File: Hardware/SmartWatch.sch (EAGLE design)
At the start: 99 parts, among them IC1 BQ25180YBGR, IC2 DRV2605YZFR, IC3 BMA421, IC9 RT6160AWSC, J1 503480-2400, J2 TC2030-IDC, J4 KH-TYPE-C-16P, Q1 20V/4.2A/52mΩ/1.4W, Q3 SI1308EDL-T1-GE3, U1 NRF52840_QF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

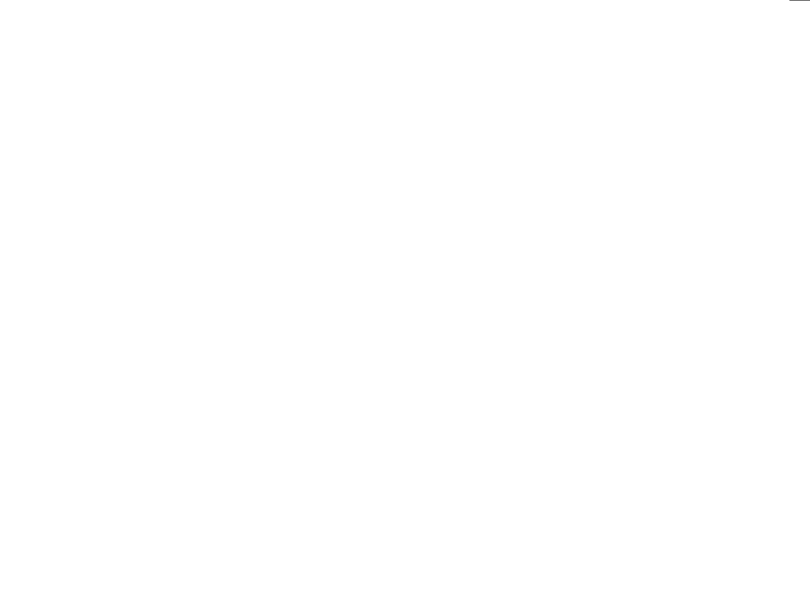
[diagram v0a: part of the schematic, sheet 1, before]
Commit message: Added the missing pads
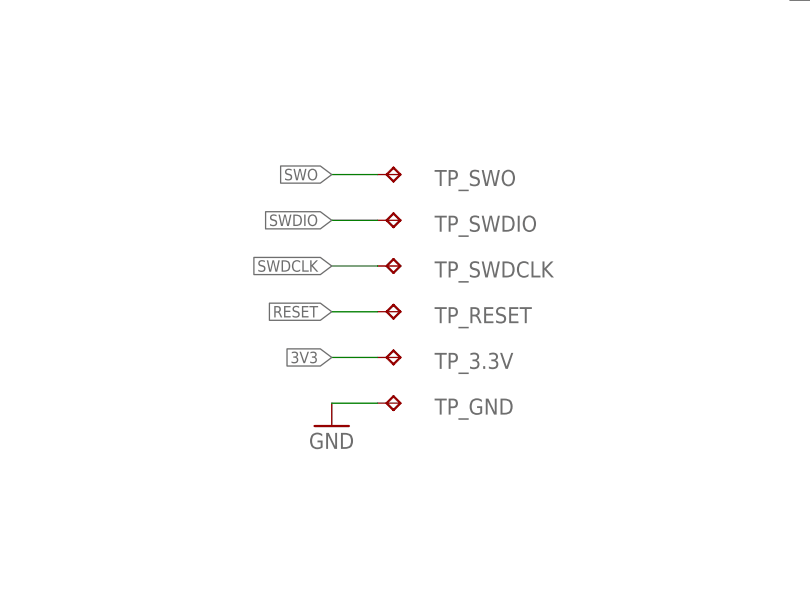
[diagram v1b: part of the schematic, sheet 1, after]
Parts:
- added TP_3.3V, TP_GND, TP_RESET, TP_SWDCLK, TP_SWDIO, TP_SWO: HECTOR_WATCH_1_TPTP20R, InkTime_v5:HECTOR_WATCH_1_TPTP20R
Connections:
- net 3V3: now also TP_3.3V.TP
- net GND: now also TP_GND.TP
- net RESET: now also TP_RESET.TP
- net SWDCLK: now also TP_SWDCLK.TP
- net SWDIO: now also TP_SWDIO.TP
- net SWO: now also TP_SWO.TP
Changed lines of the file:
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@@
 <part name="FRAME1" library="InkTime_v5" library_urn="urn:adsk.wipprod:fs.file:vf.a-hroK1ETJmXGG-M9gXLzA" deviceset="FRAMES_A3L-LOC" device=""/>
 <part name="FRAME2" library="InkTime_v5" library_urn="urn:adsk.wipprod:fs.file:vf.a-hroK1ETJmXGG-M9gXLzA" deviceset="FRAMES_A3L-LOC" device=""/>
+<part name="TP_SWO" library="InkTime_v5" library_urn="urn:adsk.wipprod:fs.file:vf.a-hroK1ETJmXGG-M9gXLzA" deviceset="HECTOR_WATCH_1_TP" device="TP20R"/>
+<part name="TP_SWDIO" library="InkTime_v5" library_urn="urn:adsk.wipprod:fs.file:vf.a-hroK1ETJmXGG-M9gXLzA" deviceset="HECTOR_WATCH_1_TP" device="TP20R"/>
+<part name="TP_SWDCLK" library="InkTime_v5" library_urn="urn:adsk.wipprod:fs.file:vf.a-hroK1ETJmXGG-M9gXLzA" deviceset="HECTOR_WATCH_1_TP" device="TP20R"/>
+<part name="TP_RESET" library="InkTime_v5" library_urn="urn:adsk.wipprod:fs.file:vf.a-hroK1ETJmXGG-M9gXLzA" deviceset="HECTOR_WATCH_1_TP" device="TP20R"/>
+<part name="TP_3.3V" library="InkTime_v5" library_urn="urn:adsk.wipprod:fs.file:vf.a-hroK1ETJmXGG-M9gXLzA" deviceset="HECTOR_WATCH_1_TP" device="TP20R"/>
+<part name="TP_GND" library="InkTime_v5" library_urn="urn:adsk.wipprod:fs.file:vf.a-hroK1ETJmXGG-M9gXLzA" deviceset="HECTOR_WATCH_1_TP" device="TP20R"/>
+<part name="GND61" library="InkTime_v5" library_urn="urn:adsk.wipprod:fs.file:vf.a-hroK1ETJmXGG-M9gXLzA" deviceset="SUPPLY1_GND" device="" value="GND"/>
 </parts>
 <sheets>
@@
 <attribute name="SHEET" x="357.505" y="5.08" size="2.54" layer="94"/>
 </instance>
+<instance part="TP_SWO" gate="G$1" x="172.72" y="53.34" smashed="yes" rot="R270">
+<attribute name="NAME" x="176.53" y="52.07" size="1.778" layer="95"/>
+<attribute name="TP_SIGNAL_NAME" x="171.45" y="52.07" size="1.778" layer="97" rot="R270"/>
+</instance>
+<instance part="TP_SWDIO" gate="G$1" x="172.72" y="48.26" smashed="yes" rot="R270">
+<attribute name="NAME" x="176.53" y="46.99" size="1.778" layer="95"/>
+<attribute name="TP_SIGNAL_NAME" x="171.45" y="46.99" size="1.778" layer="97" rot="R270"/>
+</instance>
+<instance part="TP_SWDCLK" gate="G$1" x="172.72" y="43.18" smashed="yes" rot="R270">
+<attribute name="NAME" x="176.53" y="41.91" size="1.778" layer="95"/>
+<attribute name="TP_SIGNAL_NAME" x="171.45" y="41.91" size="1.778" layer="97" rot="R270"/>
+</instance>
+<instance part="TP_RESET" gate="G$1" x="172.72" y="38.1" smashed="yes" rot="R270">
+<attribute name="NAME" x="176.53" y="36.83" size="1.778" layer="95"/>
+<attribute name="TP_SIGNAL_NAME" x="171.45" y="36.83" size="1.778" layer="97" rot="R270"/>
+</instance>
+<instance part="TP_3.3V" gate="G$1" x="172.72" y="33.02" smashed="yes" rot="R270">
+<attribute name="NAME" x="176.53" y="31.75" size="1.778" layer="95"/>
+<attribute name="TP_SIGNAL_NAME" x="171.45" y="31.75" size="1.778" layer="97" rot="R270"/>
+</instance>
+<instance part="TP_GND" gate="G$1" x="172.72" y="27.94" smashed="yes" rot="R270">
+<attribute name="NAME" x="176.53" y="26.67" size="1.778" layer="95"/>
+<attribute name="TP_SIGNAL_NAME" x="171.45" y="26.67" size="1.778" layer="97" rot="R270"/>
+</instance>
+<instance part="GND61" gate="1" x="165.1" y="25.4" smashed="yes">
+<attribute name="VALUE" x="162.56" y="22.86" size="1.778" layer="96"/>
+</instance>
 </instances>
 <busses>
@@
 <junction x="345.44" y="160.02"/>
 <pinref part="GND57" gate="1" pin="GND"/>
+</segment>
+<segment>
+<pinref part="TP_GND" gate="G$1" pin="TP"/>
+<wire x1="170.18" y1="27.94" x2="165.1" y2="27.94" width="0.1524" layer="91"/>
+<pinref part="GND61" gate="1" pin="GND"/>
 </segment>
 </net>
@@
 <label x="281.94" y="121.92" size="1.27" layer="95" xref="yes"/>
 </segment>
+<segment>
+<pinref part="TP_SWDIO" gate="G$1" pin="TP"/>
+<wire x1="170.18" y1="48.26" x2="165.1" y2="48.26" width="0.1524" layer="91"/>
+<label x="165.1" y="48.26" size="1.27" layer="95" rot="R180" xref="yes"/>
+</segment>
 </net>
 <net name="SWDCLK" class="0">
@@
 <label x="281.94" y="119.38" size="1.27" layer="95" xref="yes"/>
 </segment>
+<segment>
+<pinref part="TP_SWDCLK" gate="G$1" pin="TP"/>
+<wire x1="170.18" y1="43.18" x2="165.1" y2="43.18" width="0.1524" layer="91"/>
+<label x="165.1" y="43.18" size="1.27" layer="95" rot="R180" xref="yes"/>
+</segment>
 </net>
 <net name="RESET" class="0">
@@
 <label x="236.22" y="93.98" size="1.27" layer="95" rot="R270" xref="yes"/>
 </segment>
+<segment>
+<pinref part="TP_RESET" gate="G$1" pin="TP"/>
+<wire x1="170.18" y1="38.1" x2="165.1" y2="38.1" width="0.1524" layer="91"/>
+<label x="165.1" y="38.1" size="1.27" layer="95" rot="R180" xref="yes"/>
+</segment>
 </net>
 <net name="D-" class="0">
@@
 <wire x1="259.08" y1="99.06" x2="259.08" y2="93.98" width="0.1524" layer="91"/>
 <label x="259.08" y="93.98" size="1.27" layer="95" rot="R270" xref="yes"/>
+</segment>
+<segment>
+<pinref part="TP_SWO" gate="G$1" pin="TP"/>
+<wire x1="170.18" y1="53.34" x2="165.1" y2="53.34" width="0.1524" layer="91"/>
+<label x="165.1" y="53.34" size="1.27" layer="95" rot="R180" xref="yes"/>
 </segment>
 </net>
@@
 <pinref part="C7" gate="C$1" pin="1"/>
 </segment>
-</net>
+<segment>
+<pinref part="TP_3.3V" gate="G$1" pin="TP"/>
+<wire x1="170.18" y1="33.02" x2="165.1" y2="33.02" width="0.1524" layer="91"/>
+<label x="165.1" y="33.02" size="1.27" layer="95" rot="R180" xref="yes"/>
+</segment>
+</net>

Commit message: last commit probs
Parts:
- renumbered R1 to R9
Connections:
- removed net N$5: R17.2, TP_SCL.TP
- removed net N$6: R18.2, TP_SDA.TP
- removed net N$7: R17.1, R18.1
- removed net VDDH: C6.1, U1.VDD@W1, U1.VDDH@Y2
- net 3V3: now also C6.1, R17.1, R18.1, U1.VDD@W1, U1.VDDH@Y2
- net SCL: now also R17.2, TP_SCL.TP
- net SDA: now also R18.2, TP_SDA.TP
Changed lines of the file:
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@@
 </variantdefs>
 <classes>
-<class number="0" name="default" width="0" drill="0">
+<class number="0" name="default" width="0.15" drill="0">
+</class>
+<class number="1" name="POWER" width="0.3" drill="0">
 </class>
 </classes>
@@
 <part name="GND4" library="InkTime_v5" library_urn="urn:adsk.wipprod:fs.file:vf.a-hroK1ETJmXGG-M9gXLzA" deviceset="SUPPLY1_GND" device="" value="GND"/>
 <part name="GND5" library="InkTime_v5" library_urn="urn:adsk.wipprod:fs.file:vf.a-hroK1ETJmXGG-M9gXLzA" deviceset="SUPPLY1_GND" device="" value="GND"/>
-<part name="R1" library="InkTime_v5" library_urn="urn:adsk.wipprod:fs.file:vf.a-hroK1ETJmXGG-M9gXLzA" deviceset="CPF0201D7K68C1_CPF0201D7K68C1" device="" value="10K"/>
+<part name="R9" library="InkTime_v5" library_urn="urn:adsk.wipprod:fs.file:vf.a-hroK1ETJmXGG-M9gXLzA" deviceset="CPF0201D7K68C1_CPF0201D7K68C1" device="" value="10K"/>
 <part name="C37" library="InkTime_v5" library_urn="urn:adsk.wipprod:fs.file:vf.a-hroK1ETJmXGG-M9gXLzA" deviceset="NORDIC_NRF_3_CAPACITOR" device="_0402_N" value="1μF"/>
 <part name="C39" library="InkTime_v5" library_urn="urn:adsk.wipprod:fs.file:vf.a-hroK1ETJmXGG-M9gXLzA" deviceset="NORDIC_NRF_3_CAPACITOR" device="_0402_N" value="1μF"/>
@@
 <attribute name="VALUE" x="25.4" y="198.12" size="1.778" layer="96"/>
 </instance>
-<instance part="R1" gate="G$1" x="91.44" y="203.2" smashed="yes" rot="R90">
+<instance part="R9" gate="G$1" x="91.44" y="203.2" smashed="yes" rot="R90">
 <attribute name="NAME" x="90.17" y="212.09" size="1.778" layer="95" rot="R90" align="bottom-center"/>
 <attribute name="VALUE" x="92.71" y="212.09" size="1.778" layer="96" rot="R90" align="bottom-center"/>
@@
 </busses>
 <nets>
-<net name="GND" class="0">
+<net name="GND" class="1">
 <segment>
 <pinref part="IC1" gate="G$1" pin="GND"/>
@@
 <segment>
 <pinref part="GND2" gate="1" pin="GND"/>
-<pinref part="R1" gate="G$1" pin="1"/>
+<pinref part="R9" gate="G$1" pin="1"/>
 </segment>
 <segment>
@@
 <wire x1="81.28" y1="223.52" x2="91.44" y2="223.52" width="0.1524" layer="91"/>
 <wire x1="91.44" y1="223.52" x2="91.44" y2="220.98" width="0.1524" layer="91"/>
-<pinref part="R1" gate="G$1" pin="2"/>
-</segment>
-</net>
-<net name="VBAT" class="0">
+<pinref part="R9" gate="G$1" pin="2"/>
+</segment>
+</net>
+<net name="VBAT" class="1">
 <segment>
 <pinref part="IC1" gate="G$1" pin="BAT"/>
@@
 </segment>
 </net>
-<net name="VREG" class="0">
+<net name="VREG" class="1">
 <segment>
 <pinref part="C39" gate="C$1" pin="1"/>
@@
 </segment>
 <segment>
-<label x="60.96" y="93.98" size="1.4224" layer="95" xref="yes"/>
-</segment>
-<segment>
 <pinref part="IC3" gate="G$1" pin="SDX"/>
 <wire x1="88.9" y1="48.26" x2="91.44" y2="48.26" width="0.1524" layer="91"/>
@@
 <wire x1="198.12" y1="142.24" x2="193.04" y2="142.24" width="0.1524" layer="91"/>
 <label x="193.04" y="142.24" size="1.27" layer="95" rot="R180" xref="yes"/>
+</segment>
+<segment>
+<pinref part="R18" gate="G$1" pin="2"/>
+<wire x1="55.88" y1="93.98" x2="58.42" y2="93.98" width="0.1524" layer="91"/>
+<wire x1="58.42" y1="93.98" x2="60.96" y2="93.98" width="0.1524" layer="91"/>
+<junction x="58.42" y="93.98"/>
+<wire x1="58.42" y1="93.98" x2="58.42" y2="91.44" width="0.1524" layer="91"/>
+<pinref part="TP_SDA" gate="G$1" pin="TP"/>
+<label x="60.96" y="93.98" size="1.27" layer="95" xref="yes"/>
 </segment>
 </net>
@@
 <wire x1="86.36" y1="165.1" x2="93.98" y2="165.1" width="0.1524" layer="91"/>
 <label x="93.98" y="165.1" size="1.4224" layer="95" xref="yes"/>
-</segment>
-</net>
-<net name="N$5" class="0">
-<segment>
-<pinref part="R17" gate="G$1" pin="2"/>
-<wire x1="55.88" y1="101.6" x2="58.42" y2="101.6" width="0.1524" layer="91"/>
-<wire x1="58.42" y1="101.6" x2="60.96" y2="101.6" width="0.1524" layer="91"/>
-<junction x="58.42" y="101.6"/>
-<wire x1="58.42" y1="101.6" x2="58.42" y2="104.14" width="0.1524" layer="91"/>
-<pinref part="TP_SCL" gate="G$1" pin="TP"/>
-</segment>
-</net>
-<net name="N$6" class="0">
-<segment>
-<pinref part="R18" gate="G$1" pin="2"/>
-<wire x1="55.88" y1="93.98" x2="58.42" y2="93.98" width="0.1524" layer="91"/>
-<wire x1="58.42" y1="93.98" x2="60.96" y2="93.98" width="0.1524" layer="91"/>
-<junction x="58.42" y="93.98"/>
-<wire x1="58.42" y1="93.98" x2="58.42" y2="91.44" width="0.1524" layer="91"/>
-<pinref part="TP_SDA" gate="G$1" pin="TP"/>
-</segment>
-</net>
-<net name="N$7" class="0">
-<segment>
-<pinref part="R17" gate="G$1" pin="1"/>
-<wire x1="38.1" y1="101.6" x2="35.56" y2="101.6" width="0.1524" layer="91"/>
-<wire x1="35.56" y1="101.6" x2="35.56" y2="93.98" width="0.1524" layer="91"/>
-<pinref part="R18" gate="G$1" pin="1"/>
-<wire x1="38.1" y1="93.98" x2="35.56" y2="93.98" width="0.1524" layer="91"/>
-<wire x1="35.56" y1="101.6" x2="30.48" y2="101.6" width="0.1524" layer="91"/>
-<junction x="35.56" y="101.6"/>
 </segment>
 </net>
@@
 <wire x1="190.5" y1="116.84" x2="190.5" y2="114.3" width="0.1524" layer="91"/>
 <pinref part="C20" gate="C$1" pin="1"/>
-</segment>
-</net>
-<net name="VDDH" class="0">
-<segment>
-<pinref part="U1" gate="G$1" pin="VDDH@Y2"/>
-<wire x1="198.12" y1="121.92" x2="185.42" y2="121.92" width="0.1524" layer="91"/>
-<wire x1="185.42" y1="121.92" x2="185.42" y2="124.46" width="0.1524" layer="91"/>
-<pinref part="U1" gate="G$1" pin="VDD@W1"/>
-<wire x1="198.12" y1="124.46" x2="185.42" y2="124.46" width="0.1524" layer="91"/>
-<wire x1="185.42" y1="124.46" x2="175.26" y2="124.46" width="0.1524" layer="91"/>
-<wire x1="175.26" y1="124.46" x2="175.26" y2="121.92" width="0.1524" layer="91"/>
-<wire x1="175.26" y1="124.46" x2="170.18" y2="124.46" width="0.1524" layer="91"/>
-<junction x="175.26" y="124.46"/>
-<label x="170.18" y="124.46" size="1.27" layer="95" rot="R180" xref="yes"/>
-<pinref part="C6" gate="C$1" pin="1"/>
-<junction x="185.42" y="124.46"/>
 </segment>
 </net>
@@
 </segment>
 </net>
-<net name="VBUS" class="0">
+<net name="VBUS" class="1">
 <segment>
 <pinref part="IC1" gate="G$1" pin="IN"/>
@@
 </segment>
 <segment>
-<label x="60.96" y="101.6" size="1.4224" layer="95" xref="yes"/>
-</segment>
-<segment>
 <pinref part="IC3" gate="G$1" pin="SCX"/>
 <wire x1="71.12" y1="35.56" x2="71.12" y2="30.48" width="0.1524" layer="91"/>
@@
 <label x="193.04" y="139.7" size="1.27" layer="95" rot="R180" xref="yes"/>
 </segment>
-</net>
-<net name="3V3" class="0">
+<segment>
+<pinref part="R17" gate="G$1" pin="2"/>
+<wire x1="55.88" y1="101.6" x2="58.42" y2="101.6" width="0.1524" layer="91"/>
+<wire x1="58.42" y1="101.6" x2="60.96" y2="101.6" width="0.1524" layer="91"/>
+<junction x="58.42" y="101.6"/>
+<wire x1="58.42" y1="101.6" x2="58.42" y2="104.14" width="0.1524" layer="91"/>
+<pinref part="TP_SCL" gate="G$1" pin="TP"/>
+<label x="60.96" y="101.6" size="1.27" layer="95" xref="yes"/>
+</segment>
+</net>
+<net name="3V3" class="1">
 <segment>
 <pinref part="IC9" gate="G$1" pin="VOUT_2"/>
@@
 </segment>
 <segment>
-<label x="30.48" y="101.6" size="1.4224" layer="95" rot="R180" xref="yes"/>
-</segment>
-<segment>
 <pinref part="IC3" gate="G$1" pin="VDDIO"/>
 <wire x1="88.9" y1="50.8" x2="91.44" y2="50.8" width="0.1524" layer="91"/>
@@
 <wire x1="170.18" y1="33.02" x2="165.1" y2="33.02" width="0.1524" layer="91"/>
 <label x="165.1" y="33.02" size="1.27" layer="95" rot="R180" xref="yes"/>
+</segment>
+<segment>
+<pinref part="R17" gate="G$1" pin="1"/>
+<wire x1="38.1" y1="101.6" x2="33.02" y2="101.6" width="0.1524" layer="91"/>
+<pinref part="R18" gate="G$1" pin="1"/>
+<wire x1="33.02" y1="101.6" x2="30.48" y2="101.6" width="0.1524" layer="91"/>
+<wire x1="38.1" y1="93.98" x2="33.02" y2="93.98" width="0.1524" layer="91"/>
+<wire x1="33.02" y1="93.98" x2="33.02" y2="101.6" width="0.1524" layer="91"/>
+<junction x="33.02" y="101.6"/>
+<label x="30.48" y="101.6" size="1.27" layer="95" rot="R180" xref="yes"/>
+</segment>
+<segment>
+<pinref part="U1" gate="G$1" pin="VDDH@Y2"/>
+<wire x1="198.12" y1="121.92" x2="185.42" y2="121.92" width="0.1524" layer="91"/>
+<wire x1="185.42" y1="121.92" x2="185.42" y2="124.46" width="0.1524" layer="91"/>
+<pinref part="U1" gate="G$1" pin="VDD@W1"/>
+<wire x1="198.12" y1="124.46" x2="185.42" y2="124.46" width="0.1524" layer="91"/>
+<wire x1="185.42" y1="124.46" x2="175.26" y2="124.46" width="0.1524" layer="91"/>
+<wire x1="175.26" y1="124.46" x2="175.26" y2="121.92" width="0.1524" layer="91"/>
+<wire x1="175.26" y1="124.46" x2="170.18" y2="124.46" width="0.1524" layer="91"/>
+<junction x="175.26" y="124.46"/>
+<label x="170.18" y="124.46" size="1.27" layer="95" rot="R180" xref="yes"/>
+<pinref part="C6" gate="C$1" pin="1"/>
+<junction x="185.42" y="124.46"/>
 </segment>
 </net>
@@
 </segment>
 </net>
-<net name="GND" class="0">
+<net name="GND" class="1">
 <segment>
 <pinref part="D4" gate="G$1" pin="K"/>
@@
 </segment>
 </net>
-<net name="3V3" class="0">
+<net name="3V3" class="1">
 <segment>
 <pinref part="R_PWR_EPD" gate="G$1" pin="2"/>
@@
 </segment>
 </net>
-<net name="VBAT" class="0">
+<net name="VBAT" class="1">
 <segment>
 <pinref part="TP_VBAT" gate="G$1" pin="TP"/>
@@
 </segment>
 </net>
-<net name="VBUS" class="0">
+<net name="VBUS" class="1">
 <segment>
 <pinref part="D3" gate="G$1" pin="VBUS"/>
